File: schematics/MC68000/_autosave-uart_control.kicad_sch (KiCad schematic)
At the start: 3 parts, among them J11 Conn_02x20_Counter_Clockwise, J12 Conn_02x37_Row_Letter_Last, U29 74LS138

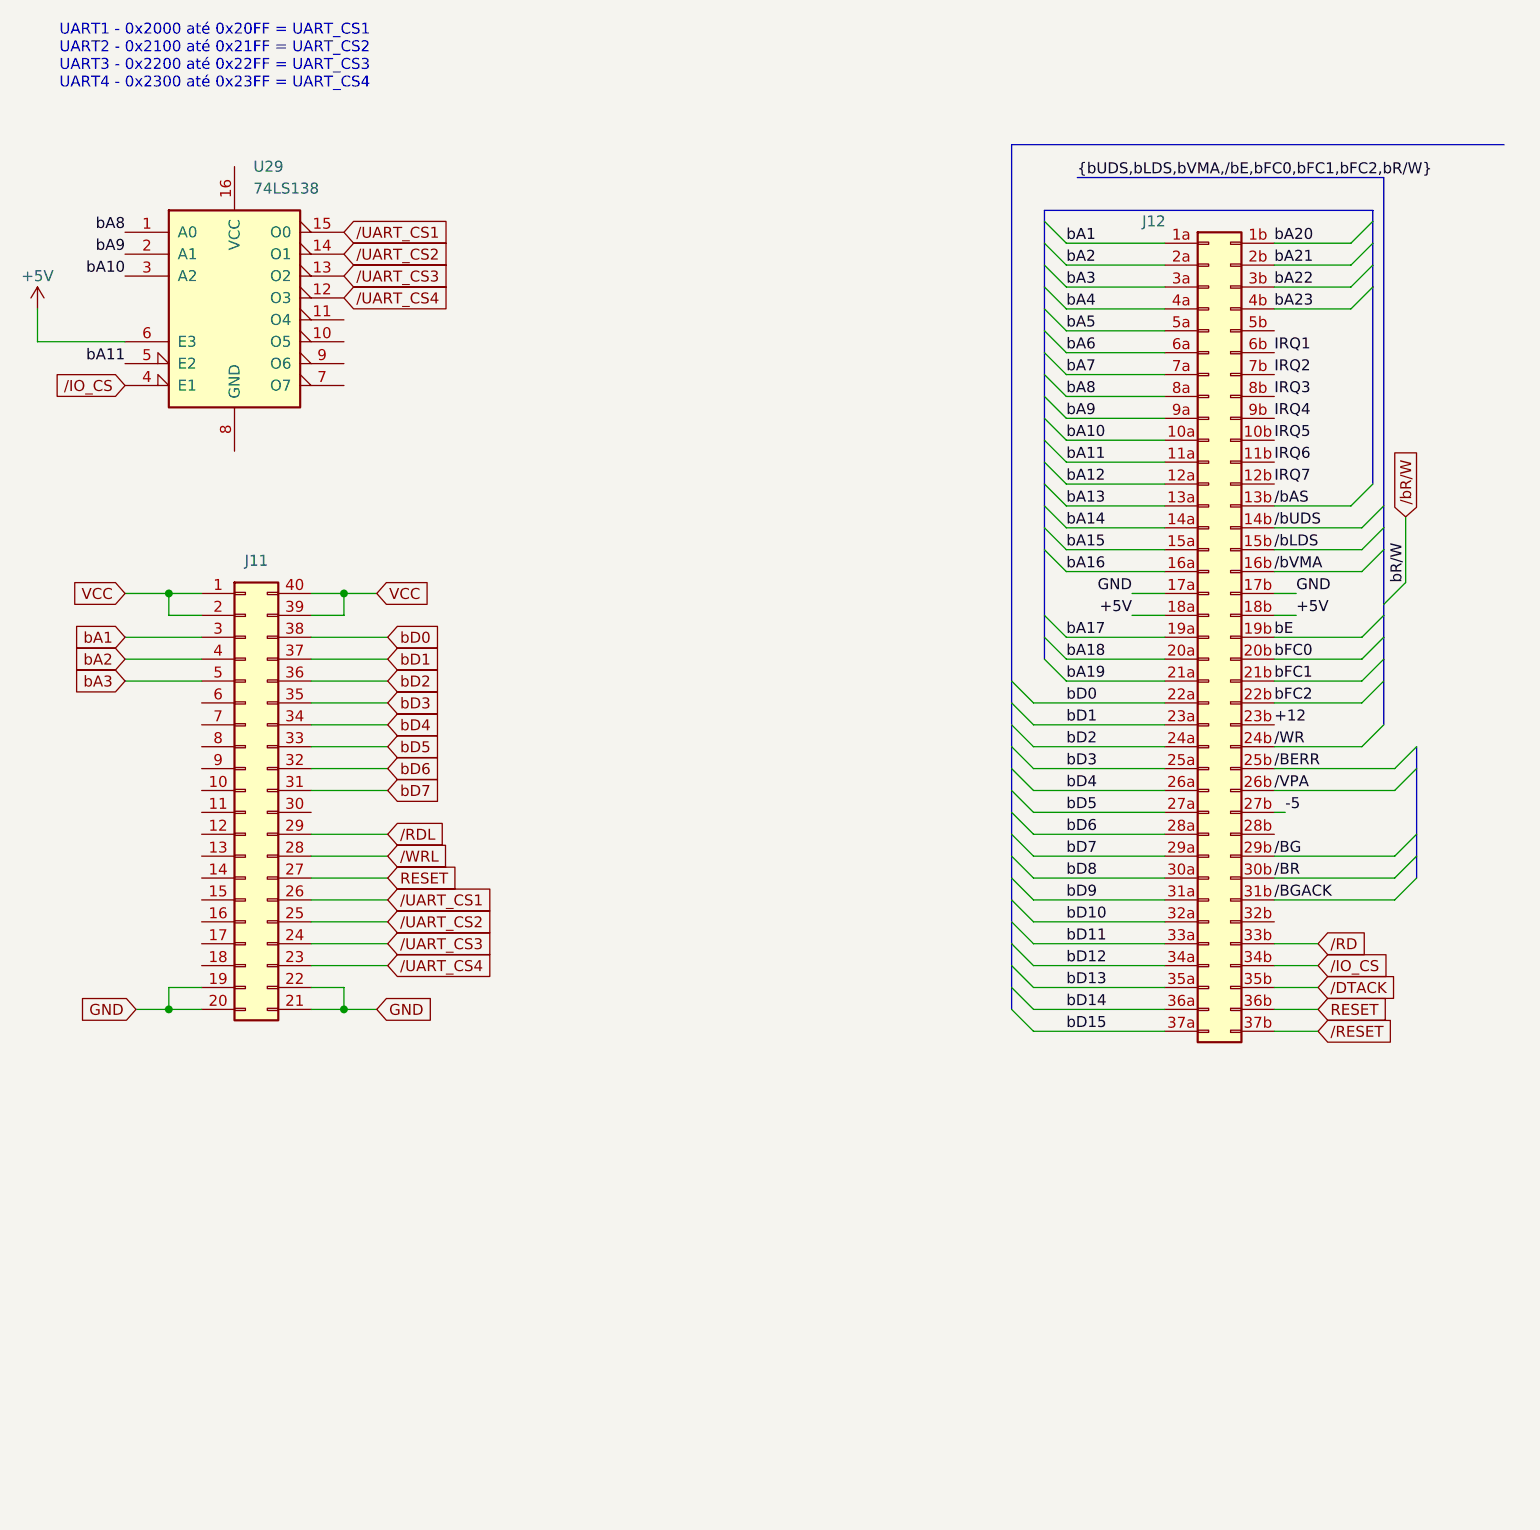
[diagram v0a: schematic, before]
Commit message: Uart reading writing with counter.asm
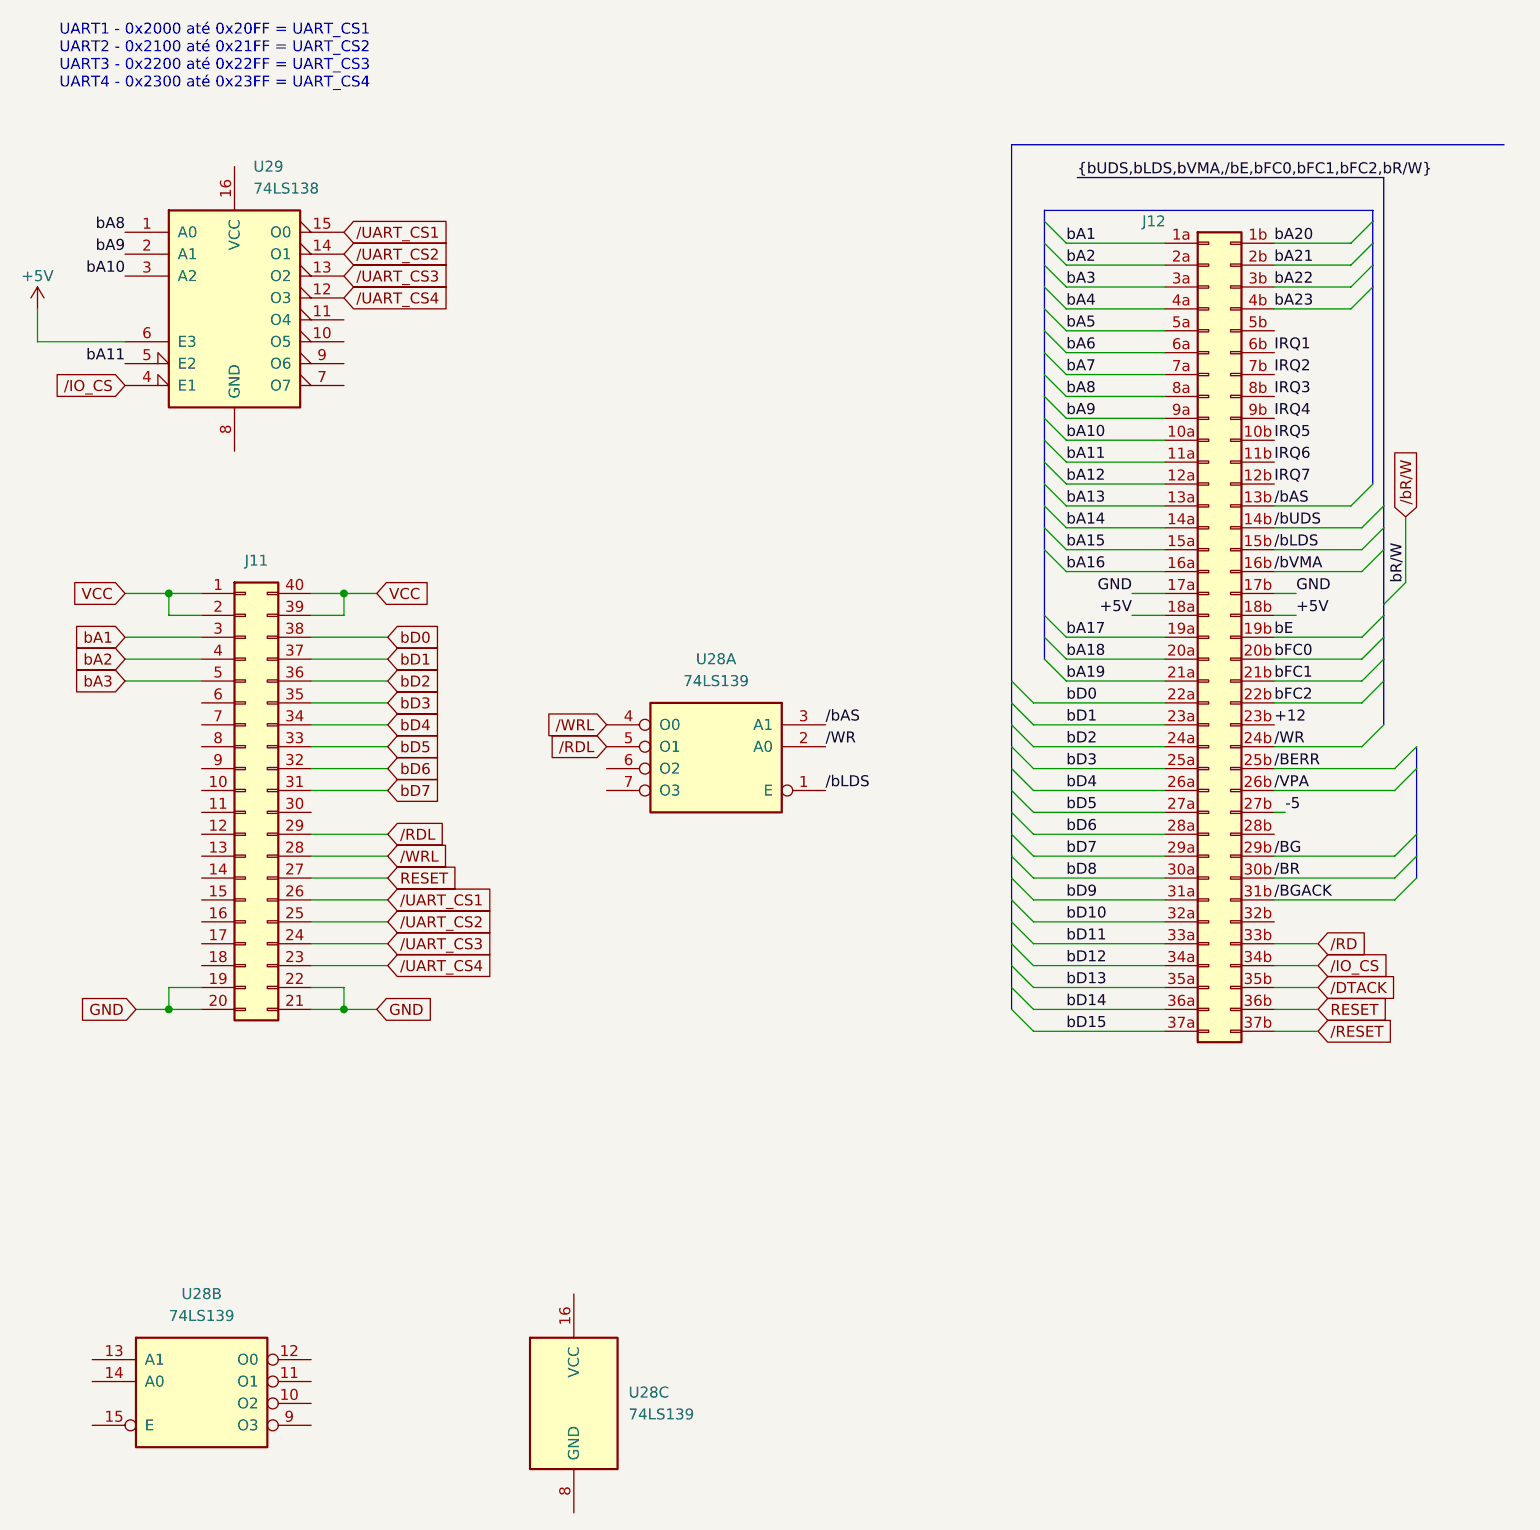
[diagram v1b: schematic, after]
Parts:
- added U28: 74LS139, symbol 74xx:74LS139
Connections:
- net /RDL: now also U28.5 (O1)
- net /WR: now also U28.2 (A0)
- net /WRL: now also U28.4 (O0)
- net /bAS: now also U28.3 (A1)
- net /bLDS: now also U28.1 (E)
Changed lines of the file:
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@@
+    (effects (font (size 1.27 1.27)) (justify left bottom))
+  )
+  (label "{slash}WR" (at 111.76 100.33 0) (fields_autoplaced)
     (effects (font (size 1.27 1.27)) (justify left bottom))
   )
@@
     (effects (font (size 1.27 1.27)) (justify left bottom))
   )
+  (label "{slash}bLDS" (at 111.76 105.41 0) (fields_autoplaced)
+    (effects (font (size 1.27 1.27)) (justify left bottom))
+  )
   (label "bA1" (at 139.7 41.91 0) (fields_autoplaced)
     (effects (font (size 1.27 1.27)) (justify left bottom))
@@
     (effects (font (size 1.27 1.27)) (justify right bottom))
   )
+  (label "{slash}bAS" (at 111.76 97.79 0) (fields_autoplaced)
+    (effects (font (size 1.27 1.27)) (justify left bottom))
+  )
   (label "bA2" (at 139.7 44.45 0) (fields_autoplaced)
     (effects (font (size 1.27 1.27)) (justify left bottom))
@@
     (property "Intersheetrefs" "${INTERSHEET_REFS}" (at 178.6081 125.73 0)
       (effects (font (size 1.27 1.27)) (justify left) hide)
+    )
+  )
+  (global_label "{slash}RDL" (shape input) (at 86.36 100.33 180) (fields_autoplaced)
+    (effects (font (size 1.27 1.27)) (justify right))
+    (property "Intersheetrefs" "${INTERSHEET_REFS}" (at 78.4762 100.33 0)
+      (effects (font (size 1.27 1.27)) (justify right) hide)
     )
   )
@@
     (property "Intersheetrefs" "${INTERSHEET_REFS}" (at 23.8662 82.55 0)
       (effects (font (size 1.27 1.27)) (justify right) hide)
+    )
+  )
+  (global_label "{slash}WRL" (shape input) (at 86.36 97.79 180) (fields_autoplaced)
+    (effects (font (size 1.27 1.27)) (justify right))
+    (property "Intersheetrefs" "${INTERSHEET_REFS}" (at 78.2948 97.79 0)
+      (effects (font (size 1.27 1.27)) (justify right) hide)
+    )
+  )
+  (symbol (lib_id "74xx:74LS139") (at 39.37 173.99 0) (unit 2)
+    (in_bom yes) (on_board yes) (dnp no) (fields_autoplaced)
+    (property "Reference" "U28" (at 39.37 163.83 0)
+      (effects (font (size 1.27 1.27)))
+    )
+    (property "Value" "74LS139" (at 39.37 166.37 0)
+      (effects (font (size 1.27 1.27)))
+    )
+    (property "Footprint" "" (at 39.37 173.99 0)
+      (effects (font (size 1.27 1.27)) hide)
+    )
+    (property "Datasheet" "http://www.ti.com/lit/ds/symlink/sn74ls139a.pdf" (at 39.37 173.99 0)
+      (effects (font (size 1.27 1.27)) hide)
+    )
+    (pin "3")
+    (pin "4")
+    (pin "5")
+    (pin "6")
+    (pin "2")
+    (pin "15")
+    (pin "12")
+    (pin "7")
+    (pin "16")
+    (pin "14")
+    (pin "9")
+    (pin "1")
+    (pin "11")
+    (pin "10")
+    (pin "13")
+    (pin "8")
+    (instances
+      (project "MC68000"
+        (path "/99c9748a-87b3-41bd-bdc2-3a5f137c7a40/95e583b5-cf01-4f04-acea-05f9c8e809c6"
+          (reference "U28") (unit 2)
+        )
+      )
     )
   )
@@
     )
   )
+  (symbol (lib_id "74xx:74LS139") (at 99.06 100.33 0) (mirror y) (unit 1)
+    (in_bom yes) (on_board yes) (dnp no)
+    (property "Reference" "U28" (at 99.06 90.17 0)
+      (effects (font (size 1.27 1.27)))
+    )
+    (property "Value" "74LS139" (at 99.06 92.71 0)
+      (effects (font (size 1.27 1.27)))
+    )
+    (property "Footprint" "" (at 99.06 100.33 0)
+      (effects (font (size 1.27 1.27)) hide)
+    )
+    (property "Datasheet" "http://www.ti.com/lit/ds/symlink/sn74ls139a.pdf" (at 99.06 100.33 0)
+      (effects (font (size 1.27 1.27)) hide)
+    )
+    (pin "3")
+    (pin "4")
+    (pin "5")
+    (pin "6")
+    (pin "2")
+    (pin "15")
+    (pin "12")
+    (pin "7")
+    (pin "16")
+    (pin "14")
+    (pin "9")
+    (pin "1")
+    (pin "11")
+    (pin "10")
+    (pin "13")
+    (pin "8")
+    (instances
+      (project "MC68000"
+        (path "/99c9748a-87b3-41bd-bdc2-3a5f137c7a40/95e583b5-cf01-4f04-acea-05f9c8e809c6"
+          (reference "U28") (unit 1)
+        )
+      )
+    )
+  )
   (symbol (lib_id "Connector_Generic:Conn_02x20_Counter_Clockwise") (at 44.45 105.41 0) (unit 1)
     (in_bom yes) (on_board yes) (dnp no) (fields_autoplaced)
@@
         )
       )
+    )
+  )
+  (symbol (lib_id "74xx:74LS139") (at 82.55 176.53 0) (unit 3)
+    (in_bom yes) (on_board yes) (dnp no) (fields_autoplaced)
+    (property "Reference" "U28" (at 88.9 175.26 0)
+      (effects (font (size 1.27 1.27)) (justify left))
+    )
+    (property "Value" "74LS139" (at 88.9 177.8 0)
+      (effects (font (size 1.27 1.27)) (justify left))
+    )
+    (property "Footprint" "" (at 82.55 176.53 0)
+      (effects (font (size 1.27 1.27)) hide)
+    )
+    (property "Datasheet" "http://www.ti.com/lit/ds/symlink/sn74ls139a.pdf" (at 82.55 176.53 0)
+      (effects (font (size 1.27 1.27)) hide)
+    )
+    (pin "3")
+    (pin "4")
+    (pin "5")
+    (pin "6")
+    (pin "2")
+    (pin "15")
+    (pin "12")
+    (pin "7")
+    (pin "16")
+    (pin "14")
+    (pin "9")
+    (pin "1")
+    (pin "11")
+    (pin "10")
+    (pin "13")
+    (pin "8")
+    (instances
+      (project "MC68000"
+        (path "/99c9748a-87b3-41bd-bdc2-3a5f137c7a40/95e583b5-cf01-4f04-acea-05f9c8e809c6"
+          (reference "U28") (unit 3)
+        )
+      )
